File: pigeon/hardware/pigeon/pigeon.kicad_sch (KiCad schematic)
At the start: 17 parts, among them J1 Battery, SW1 Power Switch, SW2 Mode Switch, U1 ESP32-S3-Zero, U2 Adafruit_Ultimate_GPS, U3 Adafruit_RFM95W

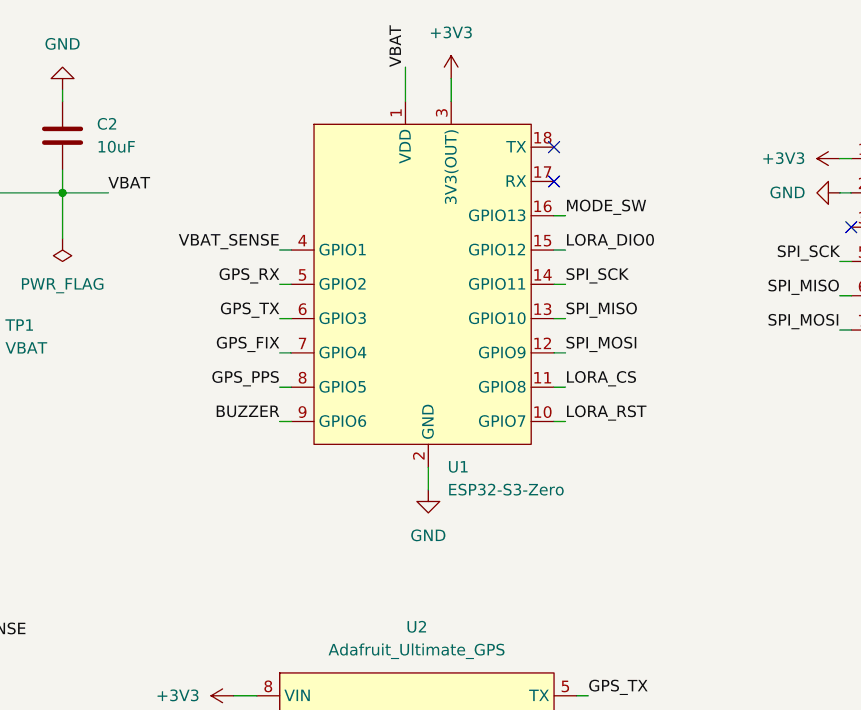
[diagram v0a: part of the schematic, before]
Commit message: pigeon: completed version 1.1 of carrier pcb. - Added rounded corners - Changed C1 to be parralel with R2 - Added mode swtich
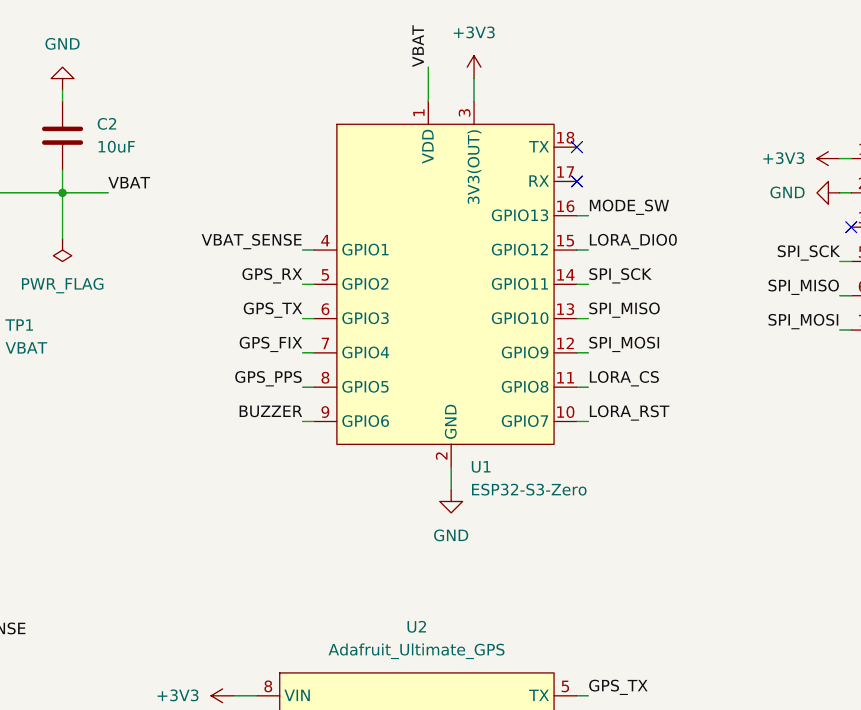
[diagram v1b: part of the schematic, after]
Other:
- moved on the sheet: U1
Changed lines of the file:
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@@
 	)
 	(no_connect
-		(at 111.76 39.37)
+		(at 114.3 39.37)
 	)
 	(no_connect
@@
 	)
 	(no_connect
-		(at 111.76 35.56)
+		(at 114.3 35.56)
 	)
 	(no_connect
@@
 	(wire
 		(pts
-			(xy 113.03 43.18) (xy 111.76 43.18)
+			(xy 115.57 43.18) (xy 114.3 43.18)
 		)
 		(stroke
@@
 	(wire
 		(pts
-			(xy 113.03 58.42) (xy 111.76 58.42)
+			(xy 115.57 58.42) (xy 114.3 58.42)
 		)
 		(stroke
@@
 	(wire
 		(pts
-			(xy 113.03 62.23) (xy 111.76 62.23)
+			(xy 115.57 62.23) (xy 114.3 62.23)
 		)
 		(stroke
@@
 	(wire
 		(pts
-			(xy 81.28 66.04) (xy 82.55 66.04)
+			(xy 83.82 66.04) (xy 85.09 66.04)
 		)
 		(stroke
@@
 	(wire
 		(pts
-			(xy 81.28 54.61) (xy 82.55 54.61)
+			(xy 83.82 54.61) (xy 85.09 54.61)
 		)
 		(stroke
@@
 	(wire
 		(pts
-			(xy 113.03 50.8) (xy 111.76 50.8)
+			(xy 115.57 50.8) (xy 114.3 50.8)
 		)
 		(stroke
@@
 	(wire
 		(pts
-			(xy 113.03 66.04) (xy 111.76 66.04)
+			(xy 115.57 66.04) (xy 114.3 66.04)
 		)
 		(stroke
@@
 	(wire
 		(pts
-			(xy 97.79 73.66) (xy 97.79 71.12)
+			(xy 100.33 73.66) (xy 100.33 71.12)
 		)
 		(stroke
@@
 	(wire
 		(pts
-			(xy 81.28 50.8) (xy 82.55 50.8)
-		)
-		(stroke
-			(width 0)
-			(type default)
-		)
-	)
-	(wire
-		(pts
-			(xy 81.28 58.42) (xy 82.55 58.42)
+			(xy 83.82 50.8) (xy 85.09 50.8)
+		)
+		(stroke
+			(width 0)
+			(type default)
+		)
+	)
+	(wire
+		(pts
+			(xy 83.82 58.42) (xy 85.09 58.42)
 		)
 		(stroke
@@
 	(wire
 		(pts
-			(xy 100.33 27.94) (xy 100.33 30.48)
-		)
-		(stroke
-			(width 0)
-			(type default)
-		)
-	)
-	(wire
-		(pts
-			(xy 81.28 62.23) (xy 82.55 62.23)
+			(xy 102.87 27.94) (xy 102.87 30.48)
+		)
+		(stroke
+			(width 0)
+			(type default)
+		)
+	)
+	(wire
+		(pts
+			(xy 83.82 62.23) (xy 85.09 62.23)
 		)
 		(stroke
@@
 	(wire
 		(pts
-			(xy 113.03 46.99) (xy 111.76 46.99)
-		)
-		(stroke
-			(width 0)
-			(type default)
-		)
-	)
-	(wire
-		(pts
-			(xy 113.03 54.61) (xy 111.76 54.61)
-		)
-		(stroke
-			(width 0)
-			(type default)
-		)
-	)
-	(wire
-		(pts
-			(xy 81.28 46.99) (xy 82.55 46.99)
+			(xy 115.57 46.99) (xy 114.3 46.99)
+		)
+		(stroke
+			(width 0)
+			(type default)
+		)
+	)
+	(wire
+		(pts
+			(xy 115.57 54.61) (xy 114.3 54.61)
+		)
+		(stroke
+			(width 0)
+			(type default)
+		)
+	)
+	(wire
+		(pts
+			(xy 83.82 46.99) (xy 85.09 46.99)
 		)
 		(stroke
@@
 	(wire
 		(pts
-			(xy 95.25 26.67) (xy 95.25 30.48)
+			(xy 97.79 26.67) (xy 97.79 30.48)
 		)
 		(stroke
@@
 	)
 	(label "SPI_MISO"
-		(at 113.03 54.61 0)
+		(at 115.57 54.61 0)
 		(effects
 			(font
@@
 	)
 	(label "LORA_RST"
-		(at 113.03 66.04 0)
+		(at 115.57 66.04 0)
 		(effects
 			(font
@@
 	)
 	(label "GPS_FIX"
-		(at 81.28 58.42 180)
+		(at 83.82 58.42 180)
 		(effects
 			(font
@@
 	)
 	(label "LORA_CS"
-		(at 113.03 62.23 0)
+		(at 115.57 62.23 0)
 		(effects
 			(font
@@
 	)
 	(label "SPI_MOSI"
-		(at 113.03 58.42 0)
+		(at 115.57 58.42 0)
 		(effects
 			(font
@@
 	)
 	(label "GPS_RX"
-		(at 81.28 50.8 180)
+		(at 83.82 50.8 180)
 		(effects
 			(font
@@
 	)
 	(label "MODE_SW"
-		(at 113.03 43.18 0)
+		(at 115.57 43.18 0)
 		(effects
 			(font
@@
 	)
 	(label "GPS_PPS"
-		(at 81.28 62.23 180)
+		(at 83.82 62.23 180)
 		(effects
 			(font
@@
 	)
 	(label "LORA_DIO0"
-		(at 113.03 46.99 0)
+		(at 115.57 46.99 0)
 		(effects
 			(font
@@
 	)
 	(label "GPS_TX"
-		(at 81.28 54.61 180)
+		(at 83.82 54.61 180)
 		(effects
 			(font
@@
 	)
 	(label "VBAT_SENSE"
-		(at 81.28 46.99 180)
+		(at 83.82 46.99 180)
 		(effects
 			(font
@@
 	)
 	(label "VBAT"
-		(at 95.25 26.67 90)
+		(at 97.79 26.67 90)
 		(effects
 			(font
@@
 	)
 	(label "SPI_SCK"
-		(at 113.03 50.8 0)
+		(at 115.57 50.8 0)
 		(effects
 			(font
@@
 	)
 	(label "BUZZER"
-		(at 81.28 66.04 180)
+		(at 83.82 66.04 180)
 		(effects
 			(font
@@
 	(symbol
 		(lib_id "power:GND")
-		(at 97.79 73.66 0)
+		(at 100.33 73.66 0)
 		(unit 1)
 		(body_style 1)
@@
 		(fields_autoplaced yes)
 		(property "Reference" "#PWR02"
-			(at 97.79 80.01 0)
+			(at 100.33 80.01 0)
 			(hide yes)
 			(show_name no)
@@
 		)
 		(property "Value" "GND"
-			(at 97.79 78.74 0)
+			(at 100.33 78.74 0)
 			(show_name no)
 			(do_not_autoplace no)
@@
 		)
 		(property "Footprint" ""
-			(at 97.79 73.66 0)
+			(at 100.33 73.66 0)
 			(hide yes)
 			(show_name no)
@@
 		)
 		(property "Datasheet" ""
-			(at 97.79 73.66 0)
+			(at 100.33 73.66 0)
 			(hide yes)
 			(show_name no)
@@
 		)
 		(property "Description" "Power symbol creates a global label with name \"GND\" , ground"
-			(at 97.79 73.66 0)
+			(at 100.33 73.66 0)
 			(hide yes)
 			(show_name no)
@@
 	(symbol
 		(lib_id "power:+3V3")
-		(at 100.33 27.94 0)
+		(at 102.87 27.94 0)
 		(unit 1)
 		(body_style 1)
@@
 		(fields_autoplaced yes)
 		(property "Reference" "#PWR03"
-			(at 100.33 31.75 0)
+			(at 102.87 31.75 0)
 			(hide yes)
 			(show_name no)
@@
 		)
 		(property "Value" "+3V3"
-			(at 100.33 22.86 0)
+			(at 102.87 22.86 0)
 			(show_name no)
 			(do_not_autoplace no)
@@
 		)
 		(property "Footprint" ""
-			(at 100.33 27.94 0)
+			(at 102.87 27.94 0)
 			(hide yes)
 			(show_name no)
@@
 		)
 		(property "Datasheet" ""
-			(at 100.33 27.94 0)
+			(at 102.87 27.94 0)
 			(hide yes)
 			(show_name no)
@@
 		)
 		(property "Description" "Power symbol creates a global label with name \"+3V3\""
-			(at 100.33 27.94 0)
+			(at 102.87 27.94 0)
 			(hide yes)
 			(show_name no)
@@
 	(symbol
 		(lib_id "AVES:ESP32-S3-Zero")
-		(at 85.09 33.02 0)
+		(at 87.63 33.02 0)
 		(unit 1)
 		(body_style 1)
@@
 		(fields_autoplaced yes)
 		(property "Reference" "U1"
-			(at 99.9333 71.12 0)
+			(at 102.4733 71.12 0)
 			(show_name no)
 			(do_not_autoplace no)
@@
 		)
 		(property "Value" "ESP32-S3-Zero"
-			(at 99.9333 73.66 0)
+			(at 102.4733 73.66 0)
 			(show_name no)
 			(do_not_autoplace no)
@@
 		)
 		(property "Footprint" "AVES:Waveshare-ESP32-S3-Zero"
-			(at 97.79 85.598 0)
+			(at 100.33 85.598 0)
 			(hide yes)
 			(show_name no)
@@
 		)
 		(property "Datasheet" "https://www.waveshare.com/wiki/ESP32-S3-Zero"
-			(at 97.79 83.566 0)
+			(at 100.33 83.566 0)
 			(hide yes)
 			(show_name no)
@@
 		)
 		(property "Description" "Waveshare ESP32-S3-Zero"
-			(at 97.79 81.788 0)
-			(hide yes)
-			(show_name no)
+			(at 100.33 81.788 0)
+			(hide yes)
+			(show_name no)
